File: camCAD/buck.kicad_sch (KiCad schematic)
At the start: 5 parts, among them J3 BATTERY, U2 SC189ZSKTRT

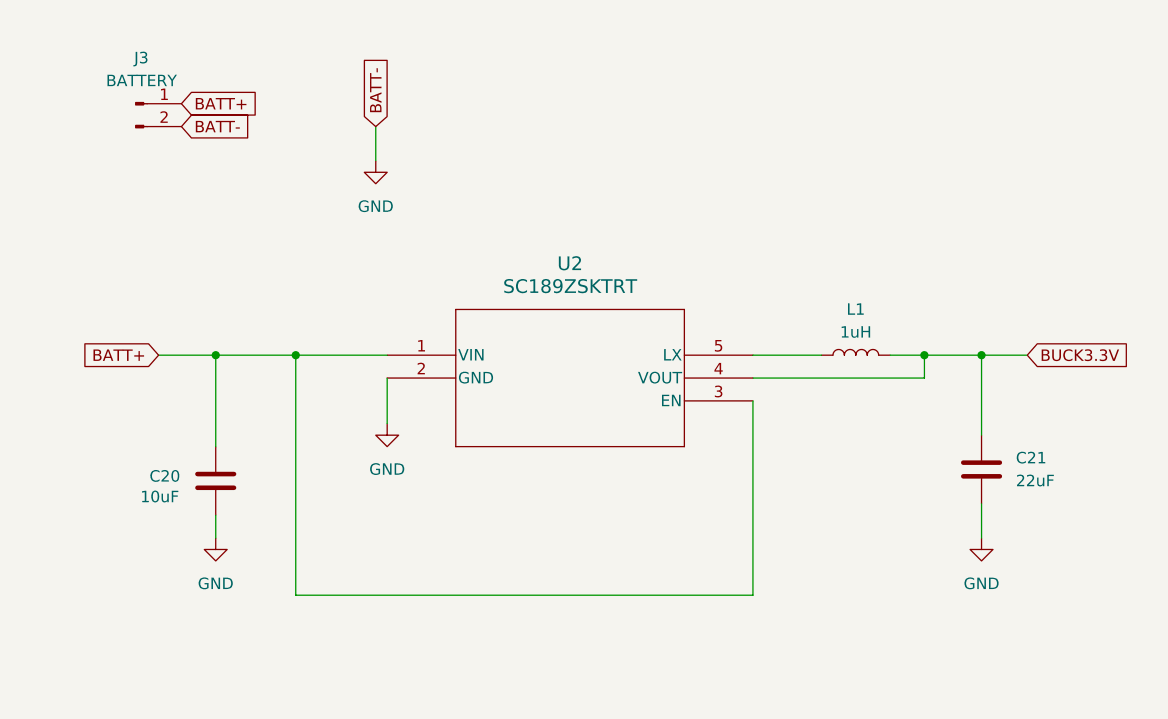
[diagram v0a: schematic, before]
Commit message: restructured hierarchy and cleaned up schematic
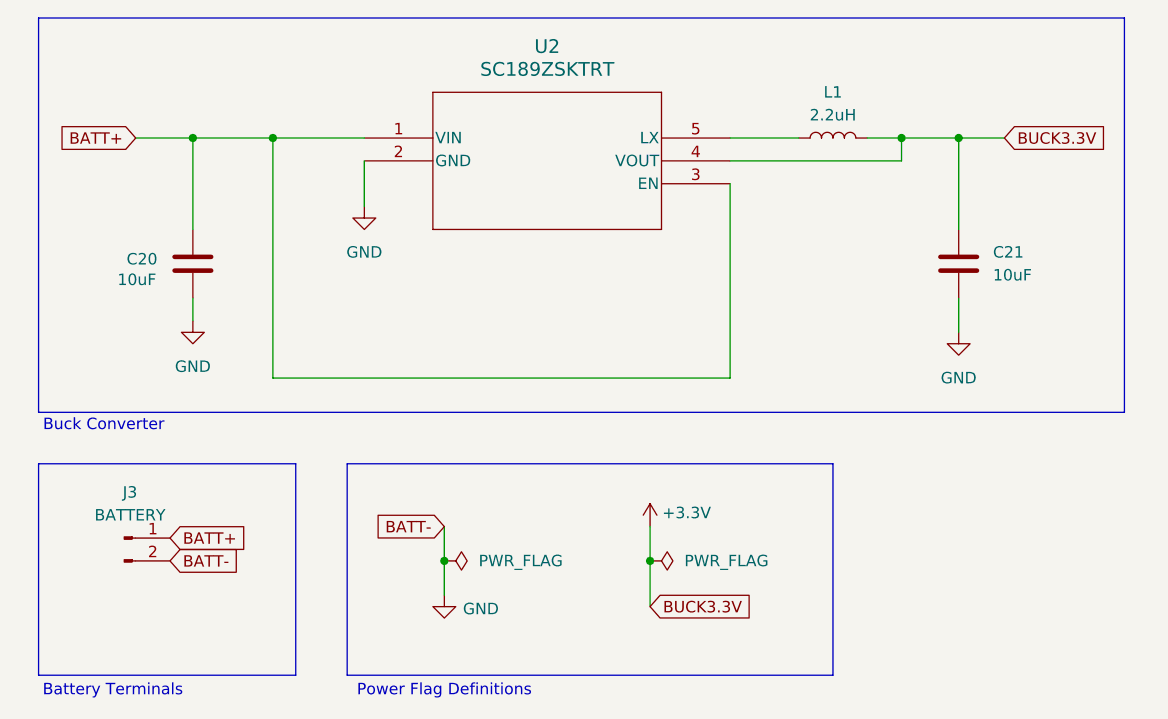
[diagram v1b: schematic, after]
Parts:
- C21: value 22uF -> 10uF
- L1: value 1uH -> 2.2uH
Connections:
- net BUCK3.3V renamed +3.3V
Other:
- note added: "Battery Terminals"
- note added: "Buck Converter"
- note added: "Power Flag Definitions"
- moved on the sheet: C20, C21, J3, L1, U2

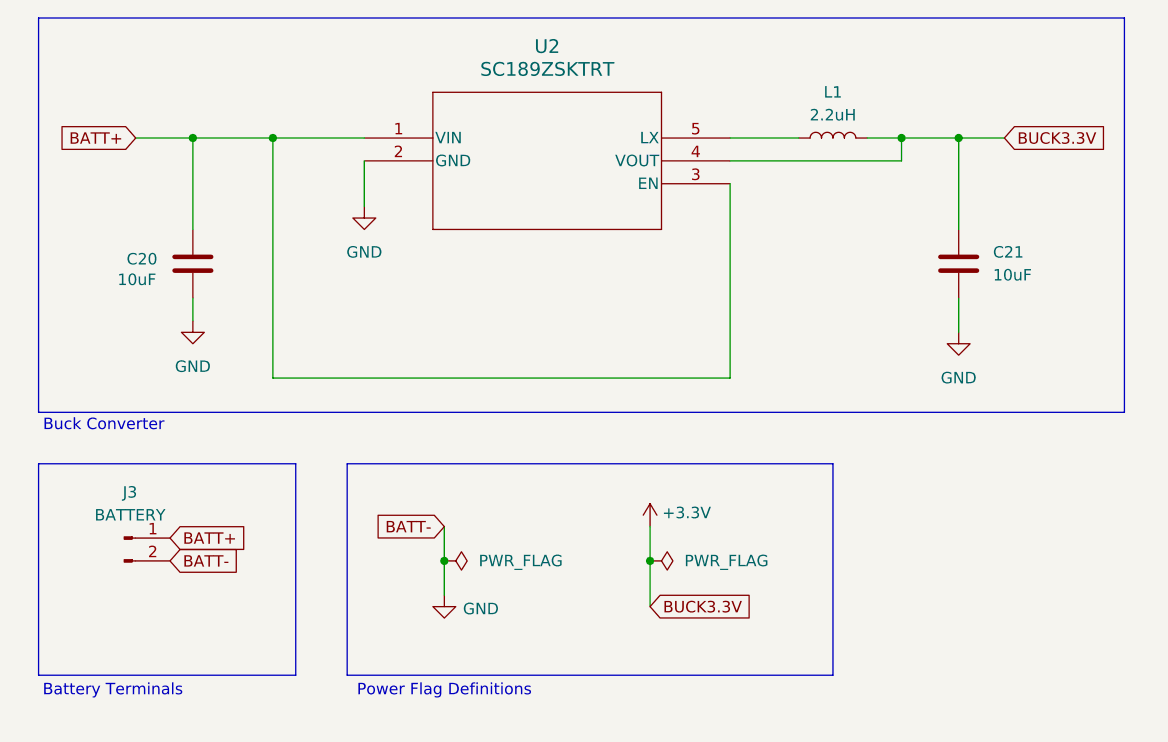
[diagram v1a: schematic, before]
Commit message: Added battery to HardwareNotes.md, some touch ups on schematic
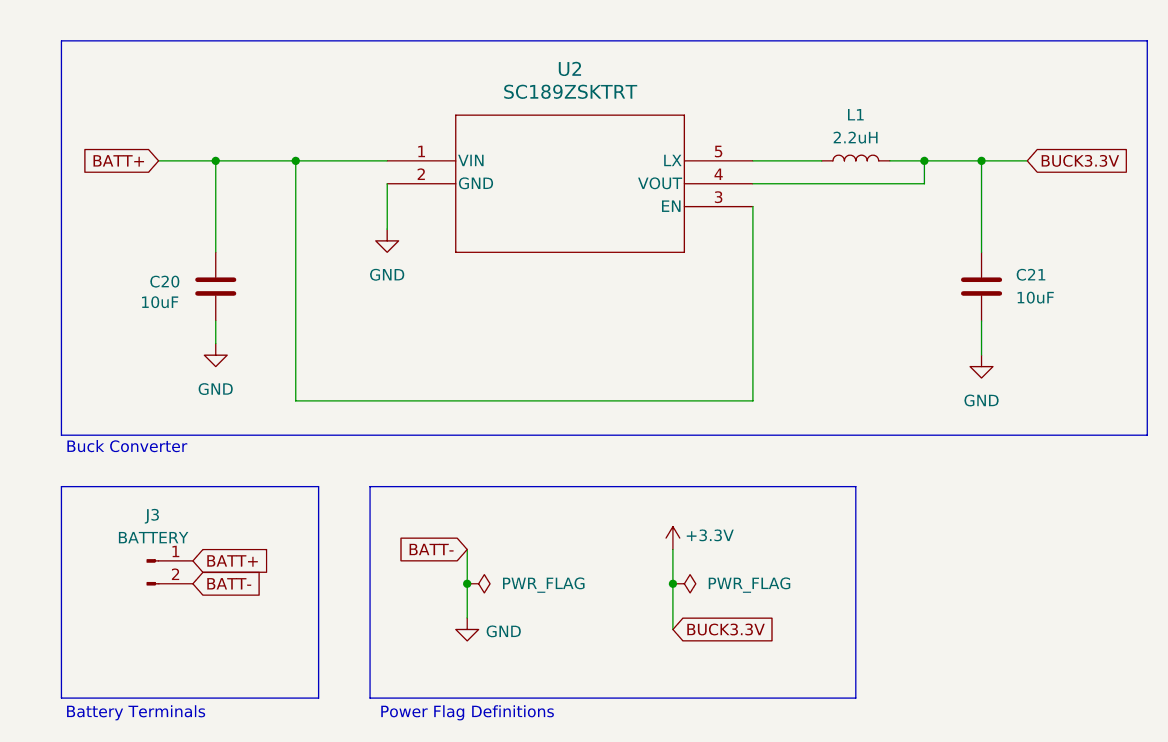
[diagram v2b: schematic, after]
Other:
- moved on the sheet: C20, C21, J3, L1, U2

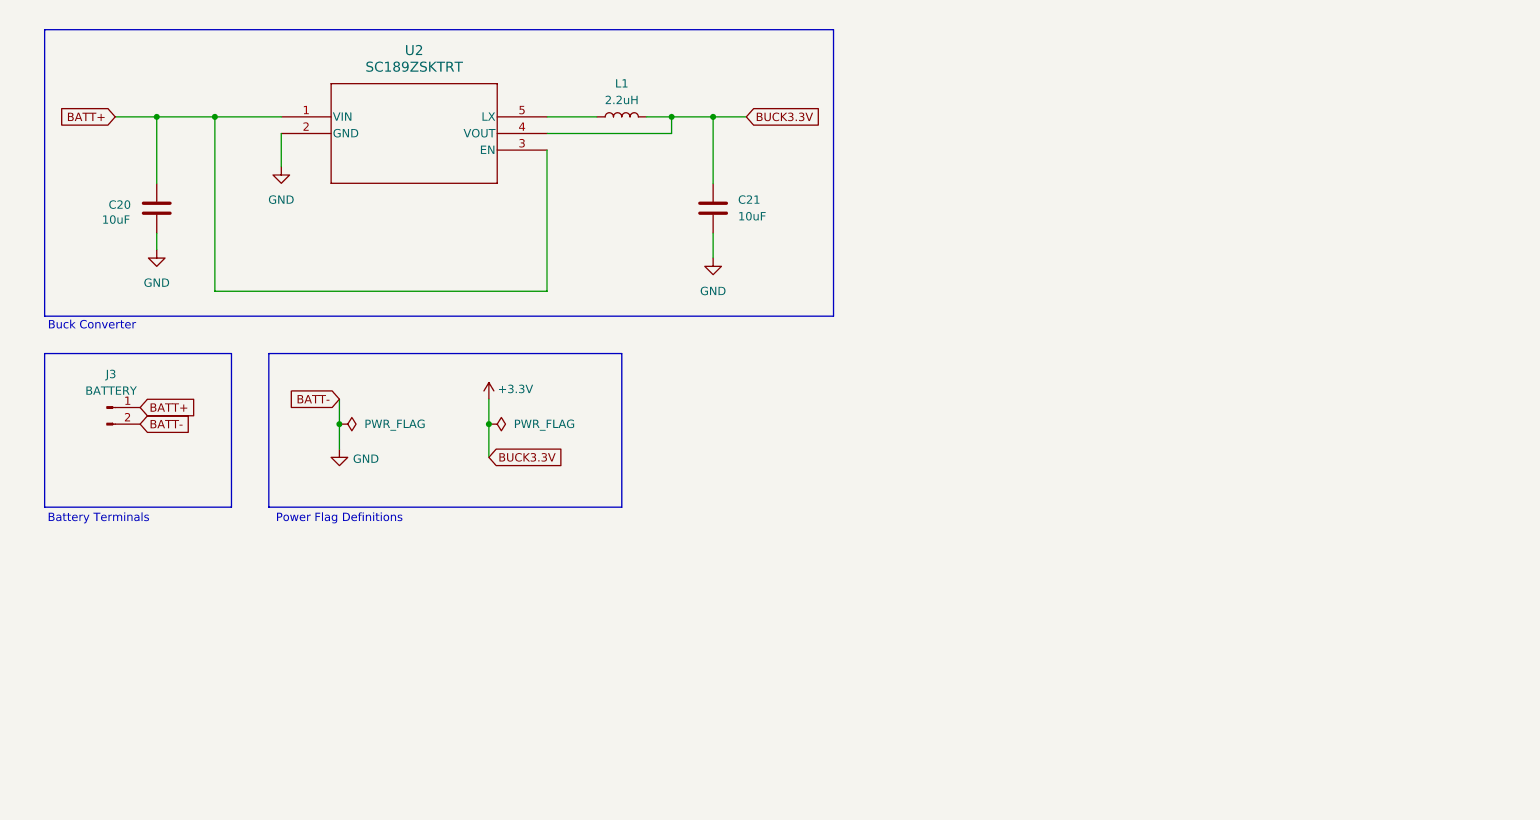
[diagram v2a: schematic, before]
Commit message: Adding charging functionality
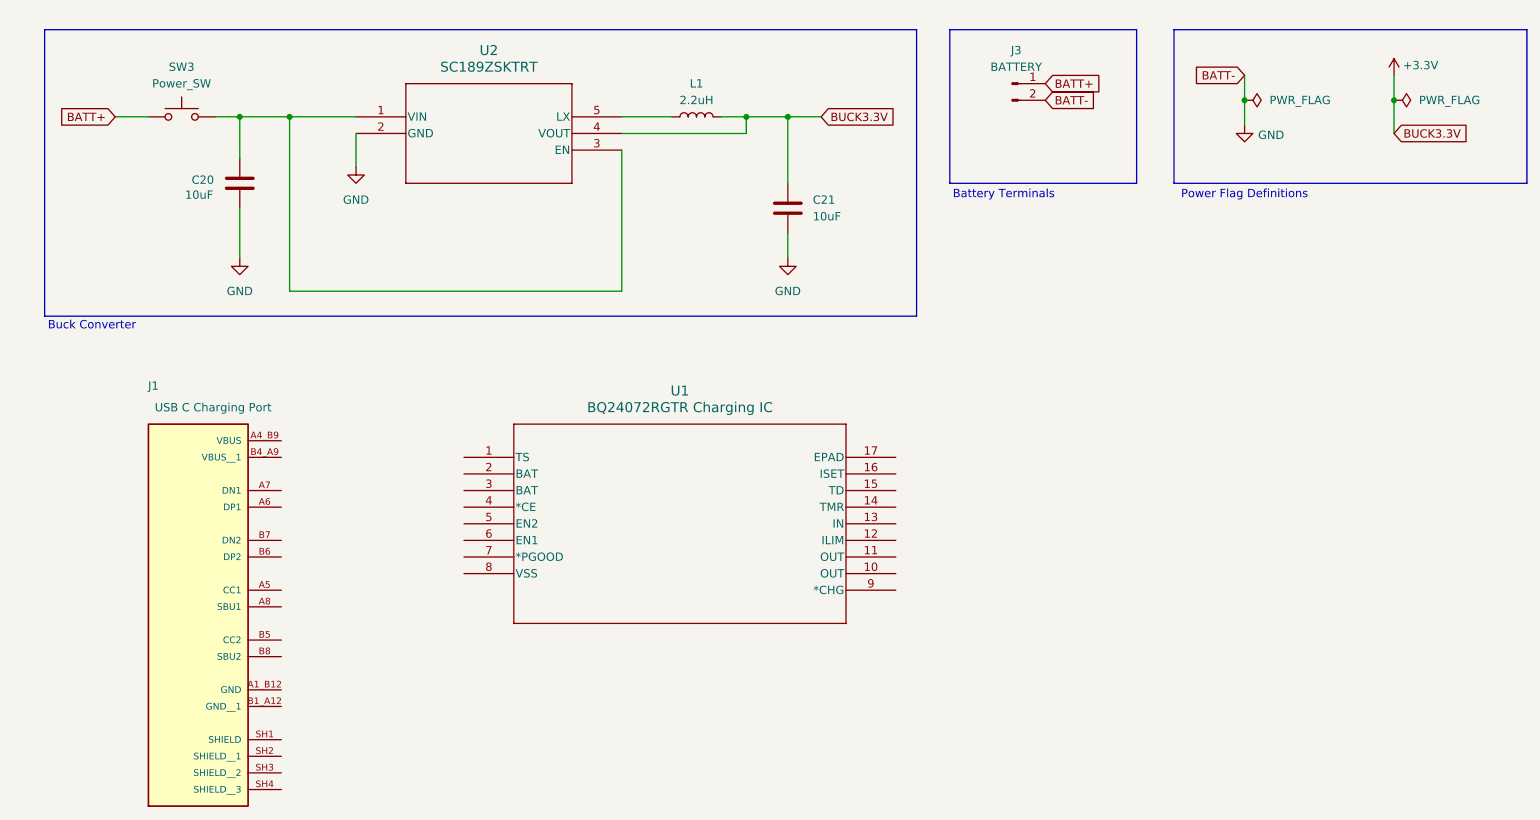
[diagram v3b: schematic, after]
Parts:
- added J1: USB C Charging Port, UJ20-C-H-G-SMT-1-P16-TR:SAMESKY_UJ20-C-H-G-SMT-1-P16-TR, symbol 1_USBC_Sockets:UJ20-C-H-G-SMT-1-P16-TR
- added SW3: Power_SW, symbol Switch:SW_Push
- added U1: BQ24072RGTR Charging IC, RGT16_1P7X1P7, symbol 1_ChargingICs:BQ24072RGTR
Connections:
- net BATT+: now also SW3.1; no longer C20.1, U2.1 (VIN), U2.3 (EN)
- new net: C20.1, SW3.2, U2.1 (VIN), U2.3 (EN)
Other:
- moved on the sheet: C20, C21, J3, L1, U2
